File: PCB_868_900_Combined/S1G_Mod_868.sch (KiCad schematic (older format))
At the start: 52 parts, among them J1 S2B-PH-K-S(LF)(SN), Q1 DMG2307L-7, SW1 CUS-12TB, T1 0732511150, U1 AP7361-33FGE-7, U2 ADF7023BCPZ, X1 ABS07-32.768KHZ-9-T, X2 ABM11-140-26.000MHZ-T3

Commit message: RF Shield and more progress
Adding an RF shield to the combined implementation of the 915MHZ version
of S1G. Also experimenting with differnt connectors and what not.
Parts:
- removed J1: S2B-PH-K-S(LF)(SN), PCB_Footprints:S2B-PH-K-S(LF)(SN), symbol S2B-PH-K-S(LF)(SN)
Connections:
- wire segments 90 -> 91
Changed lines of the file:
@@
 $EndComp
 $Comp
-L GND #PWR23
+L GND #PWR01
 U 1 1 58161058
 P 7275 6075
-F 0 "#PWR23" H 7275 5825 50  0001 C CNN
+F 0 "#PWR01" H 7275 5825 50  0001 C CNN
 F 1 "GND" H 7280 5902 50  0000 C CNN
 F 2 "" H 7275 6075 50  0000 C CNN
@@
 $EndComp
 $Comp
-L GND #PWR18
+L GND #PWR02
 U 1 1 5816222C
 P 6125 4325
-F 0 "#PWR18" H 6125 4075 50  0001 C CNN
+F 0 "#PWR02" H 6125 4075 50  0001 C CNN
 F 1 "GND" H 6130 4152 50  0000 C CNN
 F 2 "" H 6125 4325 50  0000 C CNN
@@
 $EndComp
 $Comp
-L +3.3V #PWR16
+L +3.3V #PWR03
 U 1 1 581623E1
 P 5675 2075
-F 0 "#PWR16" H 5675 1925 50  0001 C CNN
+F 0 "#PWR03" H 5675 1925 50  0001 C CNN
 F 1 "+3.3V" H 5690 2248 50  0000 C CNN
 F 2 "" H 5675 2075 50  0000 C CNN
@@
 $EndComp
 $Comp
-L GND #PWR13
+L GND #PWR04
 U 1 1 58162F98
 P 5225 3250
-F 0 "#PWR13" H 5225 3000 50  0001 C CNN
+F 0 "#PWR04" H 5225 3000 50  0001 C CNN
 F 1 "GND" H 5230 3077 50  0000 C CNN
 F 2 "" H 5225 3250 50  0000 C CNN
@@
 $EndComp
 $Comp
-L GND #PWR21
+L GND #PWR05
 U 1 1 58164E94
 P 6475 5000
-F 0 "#PWR21" H 6475 4750 50  0001 C CNN
+F 0 "#PWR05" H 6475 4750 50  0001 C CNN
 F 1 "GND" H 6480 4827 50  0000 C CNN
 F 2 "" H 6475 5000 50  0000 C CNN
@@
 $EndComp
 $Comp
-L GND #PWR24
+L GND #PWR06
 U 1 1 58165059
 P 7525 5000
-F 0 "#PWR24" H 7525 4750 50  0001 C CNN
+F 0 "#PWR06" H 7525 4750 50  0001 C CNN
 F 1 "GND" H 7530 4827 50  0000 C CNN
 F 2 "" H 7525 5000 50  0000 C CNN
@@
 $EndComp
 $Comp
-L GND #PWR22
+L GND #PWR07
 U 1 1 58165567
 P 7125 5000
-F 0 "#PWR22" H 7125 4750 50  0001 C CNN
+F 0 "#PWR07" H 7125 4750 50  0001 C CNN
 F 1 "GND" H 7130 4827 50  0000 C CNN
 F 2 "" H 7125 5000 50  0000 C CNN
@@
 $EndComp
 $Comp
-L GND #PWR27
+L GND #PWR08
 U 1 1 58168376
 P 8850 5425
-F 0 "#PWR27" H 8850 5175 50  0001 C CNN
+F 0 "#PWR08" H 8850 5175 50  0001 C CNN
 F 1 "GND" H 8855 5252 50  0000 C CNN
 F 2 "" H 8850 5425 50  0000 C CNN
@@
 $EndComp
 $Comp
-L +3.3V #PWR19
+L +3.3V #PWR09
 U 1 1 58168986
 P 6150 1275
-F 0 "#PWR19" H 6150 1125 50  0001 C CNN
+F 0 "#PWR09" H 6150 1125 50  0001 C CNN
 F 1 "+3.3V" H 6165 1448 50  0000 C CNN
 F 2 "" H 6150 1275 50  0000 C CNN
@@
 $EndComp
 $Comp
-L GND #PWR12
+L GND #PWR010
 U 1 1 58169314
 P 5225 2300
-F 0 "#PWR12" H 5225 2050 50  0001 C CNN
+F 0 "#PWR010" H 5225 2050 50  0001 C CNN
 F 1 "GND" H 5230 2127 50  0000 C CNN
 F 2 "" H 5225 2300 50  0000 C CNN
@@
 $EndComp
 $Comp
-L GND #PWR3
+L GND #PWR011
 U 1 1 58174222
 P 1525 3775
-F 0 "#PWR3" H 1525 3525 50  0001 C CNN
+F 0 "#PWR011" H 1525 3525 50  0001 C CNN
 F 1 "GND" H 1530 3602 50  0000 C CNN
 F 2 "" H 1525 3775 50  0000 C CNN
@@
 $EndComp
 $Comp
-L GND #PWR4
+L GND #PWR012
 U 1 1 581744A7
 P 2325 3775
-F 0 "#PWR4" H 2325 3525 50  0001 C CNN
+F 0 "#PWR012" H 2325 3525 50  0001 C CNN
 F 1 "GND" H 2330 3602 50  0000 C CNN
 F 2 "" H 2325 3775 50  0000 C CNN
@@
 $EndComp
 $Comp
-L GND #PWR8
+L GND #PWR013
 U 1 1 5816BC64
 P 3700 6900
-F 0 "#PWR8" H 3700 6650 50  0001 C CNN
+F 0 "#PWR013" H 3700 6650 50  0001 C CNN
 F 1 "GND" H 3705 6727 50  0000 C CNN
 F 2 "" H 3700 6900 50  0000 C CNN
@@
 $EndComp
 $Comp
-L GND #PWR15
+L GND #PWR014
 U 1 1 5816BFC1
 P 5575 6900
-F 0 "#PWR15" H 5575 6650 50  0001 C CNN
+F 0 "#PWR014" H 5575 6650 50  0001 C CNN
 F 1 "GND" H 5580 6727 50  0000 C CNN
 F 2 "" H 5575 6900 50  0000 C CNN
@@
 $EndComp
 $Comp
-L +3.3V #PWR14
+L +3.3V #PWR015
 U 1 1 5816C55D
 P 5575 6450
-F 0 "#PWR14" H 5575 6300 50  0001 C CNN
+F 0 "#PWR015" H 5575 6300 50  0001 C CNN
 F 1 "+3.3V" H 5590 6623 50  0000 C CNN
 F 2 "" H 5575 6450 50  0000 C CNN
@@
 $EndComp
 $Comp
-L GND #PWR20
+L GND #PWR016
 U 1 1 58175F58
 P 6450 1775
-F 0 "#PWR20" H 6450 1525 50  0001 C CNN
+F 0 "#PWR016" H 6450 1525 50  0001 C CNN
 F 1 "GND" H 6455 1602 50  0000 C CNN
 F 2 "" H 6450 1775 50  0000 C CNN
@@
 $EndComp
 $Comp
-L GND #PWR25
+L GND #PWR017
 U 1 1 581763CA
 P 7950 1775
-F 0 "#PWR25" H 7950 1525 50  0001 C CNN
+F 0 "#PWR017" H 7950 1525 50  0001 C CNN
 F 1 "GND" H 7955 1602 50  0000 C CNN
 F 2 "" H 7950 1775 50  0000 C CNN
@@
 $EndComp
 $Comp
-L GND #PWR9
+L GND #PWR018
 U 1 1 5817CEBD
 P 3925 2150
-F 0 "#PWR9" H 3925 1900 50  0001 C CNN
+F 0 "#PWR018" H 3925 1900 50  0001 C CNN
 F 1 "GND" H 3930 1977 50  0000 C CNN
 F 2 "" H 3925 2150 50  0000 C CNN
@@
 $EndComp
 $Comp
-L GND #PWR11
+L GND #PWR019
 U 1 1 5817CF2D
 P 4725 2150
-F 0 "#PWR11" H 4725 1900 50  0001 C CNN
+F 0 "#PWR019" H 4725 1900 50  0001 C CNN
 F 1 "GND" H 4730 1977 50  0000 C CNN
 F 2 "" H 4725 2150 50  0000 C CNN
@@
 $EndComp
 $Comp
-L +3.3V #PWR6
+L +3.3V #PWR020
 U 1 1 5817CF98
 P 3425 1700
-F 0 "#PWR6" H 3425 1550 50  0001 C CNN
+F 0 "#PWR020" H 3425 1550 50  0001 C CNN
 F 1 "+3.3V" H 3440 1873 50  0000 C CNN
 F 2 "" H 3425 1700 50  0000 C CNN
@@
 $EndComp
 $Comp
-L GND #PWR5
+L GND #PWR021
 U 1 1 5818E84F
 P 3125 3775
-F 0 "#PWR5" H 3125 3525 50  0001 C CNN
+F 0 "#PWR021" H 3125 3525 50  0001 C CNN
 F 1 "GND" H 3130 3602 50  0000 C CNN
 F 2 "" H 3125 3775 50  0000 C CNN
@@
 $EndComp
 $Comp
-L GND #PWR10
+L GND #PWR022
 U 1 1 58195E9E
 P 4525 4050
-F 0 "#PWR10" H 4525 3800 50  0001 C CNN
+F 0 "#PWR022" H 4525 3800 50  0001 C CNN
 F 1 "GND" H 4530 3877 50  0000 C CNN
 F 2 "" H 4525 4050 50  0000 C CNN
@@
 $EndComp
 $Comp
-L GND #PWR7
+L GND #PWR023
 U 1 1 58196935
 P 3650 2975
-F 0 "#PWR7" H 3650 2725 50  0001 C CNN
+F 0 "#PWR023" H 3650 2725 50  0001 C CNN
 F 1 "GND" H 3655 2802 50  0000 C CNN
 F 2 "" H 3650 2975 50  0000 C CNN
@@
 $EndComp
 $Comp
-L GND #PWR2
+L GND #PWR024
 U 1 1 581979F7
 P 1000 4050
-F 0 "#PWR2" H 1000 3800 50  0001 C CNN
+F 0 "#PWR024" H 1000 3800 50  0001 C CNN
 F 1 "GND" H 1005 3877 50  0000 C CNN
 F 2 "" H 1000 4050 50  0000 C CNN
@@
 $EndComp
 $Comp
-L +3.3V #PWR26
+L +3.3V #PWR025
 U 1 1 581AA58C
 P 8625 2550
-F 0 "#PWR26" H 8625 2400 50  0001 C CNN
+F 0 "#PWR025" H 8625 2400 50  0001 C CNN
 F 1 "+3.3V" H 8640 2723 50  0000 C CNN
 F 2 "" H 8625 2550 50  0000 C CNN
@@
 F7 "SYNC" I L 9650 3650 60
 F8 "VBUS" I L 9650 3750 60
+F9 "VIN" I L 9650 3850 60
 $EndSheet
 $Comp
@@
 $EndComp
 $Comp
-L S2B-PH-K-S(LF)(SN) J1
-U 1 1 58229495
-P 750 6450
-F 0 "J1" H 700 6725 60  0000 C CNN
-F 1 "S2B-PH-K-S(LF)(SN)" H 1150 6650 60  0000 C CNN
-F 2 "PCB_Footprints:S2B-PH-K-S(LF)(SN)" H 600 6525 60  0001 C CNN
-F 3 "http://www.jst-mfg.com/product/pdf/eng/ePH.pdf" H 475 6825 60  0001 C CNN
-F 4 "0.06152 @ 5000" H 575 6925 60  0001 C CNN "Cost"
-F 5 "9 Sept 2016" H 675 7025 60  0001 C CNN "Date Created "
-F 6 "9 Sept 2016" H 775 7125 60  0001 C CNN "Date Modified"
-F 7 "Adam Vadala-Roth" H 875 7225 60  0001 C CNN "Designer "
-F 8 "5.5mm" H 975 7325 60  0001 C CNN "Height"
-F 9 "Yes" H 1075 7425 60  0001 C CNN "RHoS?"
-F 10 "JST Sales America Inc" H 1175 7525 60  0001 C CNN "MFR"
-F 11 "S2B-PH-K-S(LF)(SN)" H 1275 7625 60  0001 C CNN "MFR#"
-F 12 "Through Hole" H 1375 7725 60  0001 C CNN "Mounting"
-F 13 "2" H 1475 7825 60  0001 C CNN "Pin Count#"
-F 14 "Active" H 1575 7925 60  0001 C CNN "Status"
-F 15 "N/A" H 1675 8025 60  0001 C CNN "Tolerance"
-F 16 "Through Hole right angle connector." H 1775 8125 60  0001 C CNN "Type"
-F 17 "N/A" H 1875 8225 60  0001 C CNN "Voltage"
-F 18 "N/A" H 1975 8325 60  0001 C CNN "Wattage"
-F 19 "N/A" H 2075 8425 60  0001 C CNN "Component-Value"
-F 20 "2 Positions Header, Shrouded Connector 0.079\" (2.00mm) Through Hole, Right Angle Tin" H 2175 8525 60  0001 C CNN "Description"
-	1    750  6450
-	1    0    0    1
-$EndComp
-$Comp
 L M2.5_Hole H1
 U 1 1 58229636
@@
 NoConn ~ 10350 6050
 $Comp
-L GND #PWR17
+L GND #PWR026
 U 1 1 5822EA21
 P 5750 7525
-F 0 "#PWR17" H 5750 7275 50  0001 C CNN
+F 0 "#PWR026" H 5750 7275 50  0001 C CNN
 F 1 "GND" H 5755 7352 50  0000 C CNN
 F 2 "" H 5750 7525 50  0000 C CNN
@@
 $EndComp
 $Comp
-L GND #PWR1
+L GND #PWR027
 U 1 1 582360D6
 P 950 6525
-F 0 "#PWR1" H 950 6275 50  0001 C CNN
+F 0 "#PWR027" H 950 6275 50  0001 C CNN
 F 1 "GND" H 955 6352 50  0000 C CNN
 F 2 "" H 950 6525 50  0000 C CNN
@@
 	3125 3000 3125 3325
 Connection ~ 3425 2550
+Text Label 9300 3850 0    60   ~ 0
+PSU_IN
+Wire Wire Line
+	9225 3850 9650 3850
 $EndSCHEMATC

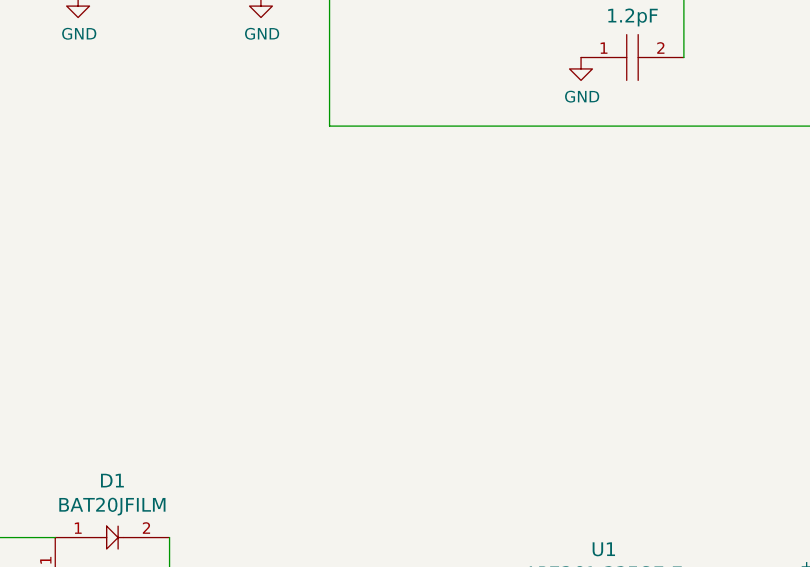
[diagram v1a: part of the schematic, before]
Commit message: First pass on PCB
First pass on PCB completed. PCB_868_900_Combined is the folder for the
finished rev.
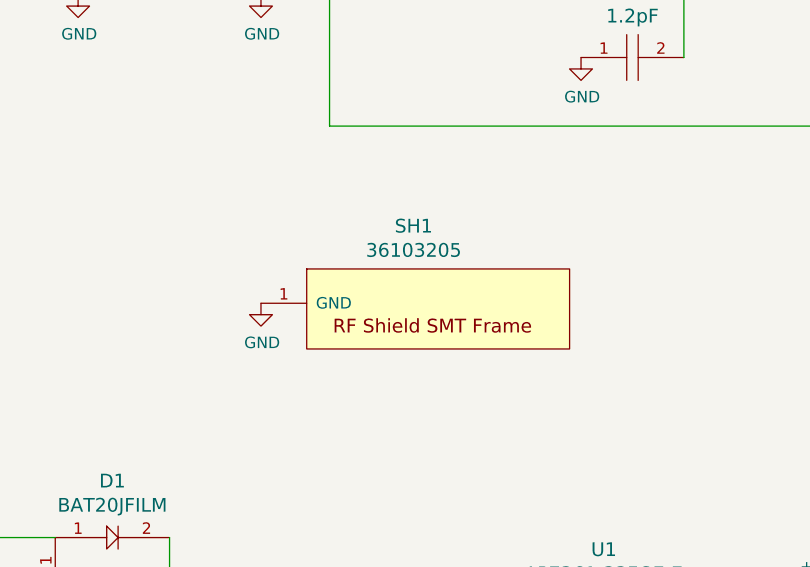
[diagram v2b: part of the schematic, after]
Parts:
- added SH1: 36103205, PCB_Footprints:36103205, symbol 36103205
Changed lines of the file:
@@
 $EndComp
 $Comp
-L GND #PWR01
+L GND #PWR24
 U 1 1 58161058
 P 7275 6075
-F 0 "#PWR01" H 7275 5825 50  0001 C CNN
+F 0 "#PWR24" H 7275 5825 50  0001 C CNN
 F 1 "GND" H 7280 5902 50  0000 C CNN
 F 2 "" H 7275 6075 50  0000 C CNN
@@
 $EndComp
 $Comp
-L GND #PWR02
+L GND #PWR19
 U 1 1 5816222C
 P 6125 4325
-F 0 "#PWR02" H 6125 4075 50  0001 C CNN
+F 0 "#PWR19" H 6125 4075 50  0001 C CNN
 F 1 "GND" H 6130 4152 50  0000 C CNN
 F 2 "" H 6125 4325 50  0000 C CNN
@@
 $EndComp
 $Comp
-L +3.3V #PWR03
+L +3.3V #PWR17
 U 1 1 581623E1
 P 5675 2075
-F 0 "#PWR03" H 5675 1925 50  0001 C CNN
+F 0 "#PWR17" H 5675 1925 50  0001 C CNN
 F 1 "+3.3V" H 5690 2248 50  0000 C CNN
 F 2 "" H 5675 2075 50  0000 C CNN
@@
 $EndComp
 $Comp
-L GND #PWR04
+L GND #PWR14
 U 1 1 58162F98
 P 5225 3250
-F 0 "#PWR04" H 5225 3000 50  0001 C CNN
+F 0 "#PWR14" H 5225 3000 50  0001 C CNN
 F 1 "GND" H 5230 3077 50  0000 C CNN
 F 2 "" H 5225 3250 50  0000 C CNN
@@
 $EndComp
 $Comp
-L GND #PWR05
+L GND #PWR22
 U 1 1 58164E94
 P 6475 5000
-F 0 "#PWR05" H 6475 4750 50  0001 C CNN
+F 0 "#PWR22" H 6475 4750 50  0001 C CNN
 F 1 "GND" H 6480 4827 50  0000 C CNN
 F 2 "" H 6475 5000 50  0000 C CNN
@@
 $EndComp
 $Comp
-L GND #PWR06
+L GND #PWR25
 U 1 1 58165059
 P 7525 5000
-F 0 "#PWR06" H 7525 4750 50  0001 C CNN
+F 0 "#PWR25" H 7525 4750 50  0001 C CNN
 F 1 "GND" H 7530 4827 50  0000 C CNN
 F 2 "" H 7525 5000 50  0000 C CNN
@@
 $EndComp
 $Comp
-L GND #PWR07
+L GND #PWR23
 U 1 1 58165567
 P 7125 5000
-F 0 "#PWR07" H 7125 4750 50  0001 C CNN
+F 0 "#PWR23" H 7125 4750 50  0001 C CNN
 F 1 "GND" H 7130 4827 50  0000 C CNN
 F 2 "" H 7125 5000 50  0000 C CNN
@@
 $EndComp
 $Comp
-L GND #PWR08
+L GND #PWR28
 U 1 1 58168376
 P 8850 5425
-F 0 "#PWR08" H 8850 5175 50  0001 C CNN
+F 0 "#PWR28" H 8850 5175 50  0001 C CNN
 F 1 "GND" H 8855 5252 50  0000 C CNN
 F 2 "" H 8850 5425 50  0000 C CNN
@@
 $EndComp
 $Comp
-L +3.3V #PWR09
+L +3.3V #PWR20
 U 1 1 58168986
 P 6150 1275
-F 0 "#PWR09" H 6150 1125 50  0001 C CNN
+F 0 "#PWR20" H 6150 1125 50  0001 C CNN
 F 1 "+3.3V" H 6165 1448 50  0000 C CNN
 F 2 "" H 6150 1275 50  0000 C CNN
@@
 $EndComp
 $Comp
-L GND #PWR010
+L GND #PWR13
 U 1 1 58169314
 P 5225 2300
-F 0 "#PWR010" H 5225 2050 50  0001 C CNN
+F 0 "#PWR13" H 5225 2050 50  0001 C CNN
 F 1 "GND" H 5230 2127 50  0000 C CNN
 F 2 "" H 5225 2300 50  0000 C CNN
@@
 $EndComp
 $Comp
-L GND #PWR011
+L GND #PWR3
 U 1 1 58174222
 P 1525 3775
-F 0 "#PWR011" H 1525 3525 50  0001 C CNN
+F 0 "#PWR3" H 1525 3525 50  0001 C CNN
 F 1 "GND" H 1530 3602 50  0000 C CNN
 F 2 "" H 1525 3775 50  0000 C CNN
@@
 $EndComp
 $Comp
-L GND #PWR012
+L GND #PWR4
 U 1 1 581744A7
 P 2325 3775
-F 0 "#PWR012" H 2325 3525 50  0001 C CNN
+F 0 "#PWR4" H 2325 3525 50  0001 C CNN
 F 1 "GND" H 2330 3602 50  0000 C CNN
 F 2 "" H 2325 3775 50  0000 C CNN
@@
 $EndComp
 $Comp
-L GND #PWR013
+L GND #PWR9
 U 1 1 5816BC64
 P 3700 6900
-F 0 "#PWR013" H 3700 6650 50  0001 C CNN
+F 0 "#PWR9" H 3700 6650 50  0001 C CNN
 F 1 "GND" H 3705 6727 50  0000 C CNN
 F 2 "" H 3700 6900 50  0000 C CNN
@@
 $EndComp
 $Comp
-L GND #PWR014
+L GND #PWR16
 U 1 1 5816BFC1
 P 5575 6900
-F 0 "#PWR014" H 5575 6650 50  0001 C CNN
+F 0 "#PWR16" H 5575 6650 50  0001 C CNN
 F 1 "GND" H 5580 6727 50  0000 C CNN
 F 2 "" H 5575 6900 50  0000 C CNN
@@
 $EndComp
 $Comp
-L +3.3V #PWR015
+L +3.3V #PWR15
 U 1 1 5816C55D
 P 5575 6450
-F 0 "#PWR015" H 5575 6300 50  0001 C CNN
+F 0 "#PWR15" H 5575 6300 50  0001 C CNN
 F 1 "+3.3V" H 5590 6623 50  0000 C CNN
 F 2 "" H 5575 6450 50  0000 C CNN
@@
 $EndComp
 $Comp
-L GND #PWR016
+L GND #PWR21
 U 1 1 58175F58
 P 6450 1775
-F 0 "#PWR016" H 6450 1525 50  0001 C CNN
+F 0 "#PWR21" H 6450 1525 50  0001 C CNN
 F 1 "GND" H 6455 1602 50  0000 C CNN
 F 2 "" H 6450 1775 50  0000 C CNN
@@
 $EndComp
 $Comp
-L GND #PWR017
+L GND #PWR26
 U 1 1 581763CA
 P 7950 1775
-F 0 "#PWR017" H 7950 1525 50  0001 C CNN
+F 0 "#PWR26" H 7950 1525 50  0001 C CNN
 F 1 "GND" H 7955 1602 50  0000 C CNN
 F 2 "" H 7950 1775 50  0000 C CNN
@@
 $EndComp
 $Comp
-L GND #PWR018
+L GND #PWR10
 U 1 1 5817CEBD
 P 3925 2150
-F 0 "#PWR018" H 3925 1900 50  0001 C CNN
+F 0 "#PWR10" H 3925 1900 50  0001 C CNN
 F 1 "GND" H 3930 1977 50  0000 C CNN
 F 2 "" H 3925 2150 50  0000 C CNN
@@
 $EndComp
 $Comp
-L GND #PWR019
+L GND #PWR12
 U 1 1 5817CF2D
 P 4725 2150
-F 0 "#PWR019" H 4725 1900 50  0001 C CNN
+F 0 "#PWR12" H 4725 1900 50  0001 C CNN
 F 1 "GND" H 4730 1977 50  0000 C CNN
 F 2 "" H 4725 2150 50  0000 C CNN
@@
 $EndComp
 $Comp
-L +3.3V #PWR020
+L +3.3V #PWR7
 U 1 1 5817CF98
 P 3425 1700
-F 0 "#PWR020" H 3425 1550 50  0001 C CNN
+F 0 "#PWR7" H 3425 1550 50  0001 C CNN
 F 1 "+3.3V" H 3440 1873 50  0000 C CNN
 F 2 "" H 3425 1700 50  0000 C CNN
@@
 $EndComp
 $Comp
-L GND #PWR021
+L GND #PWR5
 U 1 1 5818E84F
 P 3125 3775
-F 0 "#PWR021" H 3125 3525 50  0001 C CNN
+F 0 "#PWR5" H 3125 3525 50  0001 C CNN
 F 1 "GND" H 3130 3602 50  0000 C CNN
 F 2 "" H 3125 3775 50  0000 C CNN
@@
 $EndComp
 $Comp
-L GND #PWR022
+L GND #PWR11
 U 1 1 58195E9E
 P 4525 4050
-F 0 "#PWR022" H 4525 3800 50  0001 C CNN
+F 0 "#PWR11" H 4525 3800 50  0001 C CNN
 F 1 "GND" H 4530 3877 50  0000 C CNN
 F 2 "" H 4525 4050 50  0000 C CNN
@@
 $EndComp
 $Comp
-L GND #PWR023
+L GND #PWR8
 U 1 1 58196935
 P 3650 2975
-F 0 "#PWR023" H 3650 2725 50  0001 C CNN
+F 0 "#PWR8" H 3650 2725 50  0001 C CNN
 F 1 "GND" H 3655 2802 50  0000 C CNN
 F 2 "" H 3650 2975 50  0000 C CNN
@@
 $EndComp
 $Comp
-L GND #PWR024
+L GND #PWR2
 U 1 1 581979F7
 P 1000 4050
-F 0 "#PWR024" H 1000 3800 50  0001 C CNN
+F 0 "#PWR2" H 1000 3800 50  0001 C CNN
 F 1 "GND" H 1005 3877 50  0000 C CNN
 F 2 "" H 1000 4050 50  0000 C CNN
@@
 $EndComp
 $Comp
-L +3.3V #PWR025
+L +3.3V #PWR27
 U 1 1 581AA58C
 P 8625 2550
-F 0 "#PWR025" H 8625 2400 50  0001 C CNN
+F 0 "#PWR27" H 8625 2400 50  0001 C CNN
 F 1 "+3.3V" H 8640 2723 50  0000 C CNN
 F 2 "" H 8625 2550 50  0000 C CNN
@@
 NoConn ~ 10350 6050
 $Comp
-L GND #PWR026
+L GND #PWR18
 U 1 1 5822EA21
 P 5750 7525
-F 0 "#PWR026" H 5750 7275 50  0001 C CNN
+F 0 "#PWR18" H 5750 7275 50  0001 C CNN
 F 1 "GND" H 5755 7352 50  0000 C CNN
 F 2 "" H 5750 7525 50  0000 C CNN
@@
 $EndComp
 $Comp
-L GND #PWR027
+L GND #PWR1
 U 1 1 582360D6
 P 950 6525
-F 0 "#PWR027" H 950 6275 50  0001 C CNN
+F 0 "#PWR1" H 950 6275 50  0001 C CNN
 F 1 "GND" H 955 6352 50  0000 C CNN
 F 2 "" H 950 6525 50  0000 C CNN
@@
 Wire Wire Line
 	9225 3850 9650 3850
+$Comp
+L GND #PWR6
+U 1 1 5824D7CE
+P 3125 5125
+F 0 "#PWR6" H 3125 4875 50  0001 C CNN
+F 1 "GND" H 3130 4952 50  0000 C CNN
+F 2 "" H 3125 5125 50  0000 C CNN
+F 3 "" H 3125 5125 50  0000 C CNN
+	1    3125 5125
+	1    0    0    -1
+$EndComp
+$Comp
+L 36103205 SH1
+U 1 1 58250BF7
+P 3875 5125
+F 0 "SH1" H 3793 5462 60  0000 C CNN
+F 1 "36103205" H 3793 5356 60  0000 C CNN
+F 2 "PCB_Footprints:36103205" H 3225 5675 60  0001 C CNN
+F 3 "http://katalog.we-online.de/pbs/datasheet/36103205.pdf" H 3225 5775 60  0001 C CNN
+F 4 "3.49000" H 3825 5875 60  0001 C CNN "Cost"
+F 5 "9 Nov 2016" H 4025 6075 60  0001 C CNN "Date Created"
+F 6 "9 Nov 2016" H 4025 6075 60  0001 C CNN "Date Modified"
+F 7 "Adam Vadala-Roth" H 4125 6175 60  0001 C CNN "Designer"
+F 8 "2.5mm" H 4225 6275 60  0001 C CNN "Height"
+F 9 "Yes" H 4325 6375 60  0001 C CNN "RHoS?"
+F 10 "Wurth Electronics Inc" H 4425 6475 60  0001 C CNN "MFR"
+F 11 "36103205" H 4525 6575 60  0001 C CNN "MFR#"
+F 12 "SMT/SMD" H 4625 6675 60  0001 C CNN "Mounting"
+F 13 "None" H 4725 6775 60  0001 C CNN "Pin Count#"
+F 14 "Active" H 4825 6875 60  0001 C CNN "Status"
+F 15 "N/A" H 4925 6975 60  0001 C CNN "Tolerance"
+F 16 "RF Shield" H 5025 7075 60  0001 C CNN "Type"
+F 17 "N/A" H 5125 7175 60  0001 C CNN "Voltage"
+F 18 "N/A" H 5225 7275 60  0001 C CNN "Wattage"
+F 19 "N/A" H 5325 7375 60  0001 C CNN "Component-Value"
+F 20 "RF Shield Frame 0.827\" (21.00mm) X 0.827\" (21.00mm) Surface Mount" H 5425 7475 60  0001 C CNN "Description"
+	1    3875 5125
+	1    0    0    -1
+$EndComp
 $EndSCHEMATC

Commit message: Grounding and Adapter
Grounding changed on both versions of the 915MHZ/868MHZ versions of the
radio both the combined and separate antenna versions. Also an adapter
is being developed for alternative connection options.
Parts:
- removed C17, C20: CL05C180GB5NCNC, PCB_Footprints:C0402, symbol CL05C180GB5NCNC
- removed X1: ABS07-32.768KHZ-9-T, PCB_Footprints:ABS07-32.768KHZ-9-T, symbol ABS07-32.768KHZ-9-T
- added C17, C20: CL05C090CB5NNNC, PCB_Footprints:C0402, symbol CL05C090CB5NNNC
- added C33: CL10B224JO8NNNC, PCB_Footprints:C0402, symbol CL10B224JO8NNNC
- added X1: ABS05-32.768KHZ-9-T, PCB_Footprints:ABS05-32.768KHZ-9-T, symbol ABS05-32.768KHZ-9-T
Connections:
- wire segments 91 -> 93
- no-connect marks 12 -> 15

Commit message: Adapters
Adapter ended up being too large. So I split it into two separate
adapters one for SPI and one for USART over JST connectors. SPI board
has 100 ohm inline resistors for EMI and impedance matching in case the
driving device lacks these internally or on its board.  Additional
Fudicials added to the combined implementation.
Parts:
- added FD4, FD5, FD6: FIDUCIAL, PCB_Footprints:FIDUCIAL, symbol FIDUCIAL
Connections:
- no-connect marks 15 -> 18
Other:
- moved on the sheet: FD1, FD2, FD3
